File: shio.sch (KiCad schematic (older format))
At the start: 86 parts, among them J1 10118193-0001LF, U1 LM66100DCKT, U2 MAX38640AENT+, U3 NRF52840-CKAA-R7, U4 LM66100DCKT, U5 BMA400, U6 W25N01GVZEIG_TR, U8 SiP32431DR3, Y1 32.768kHz, Y3 32MHz

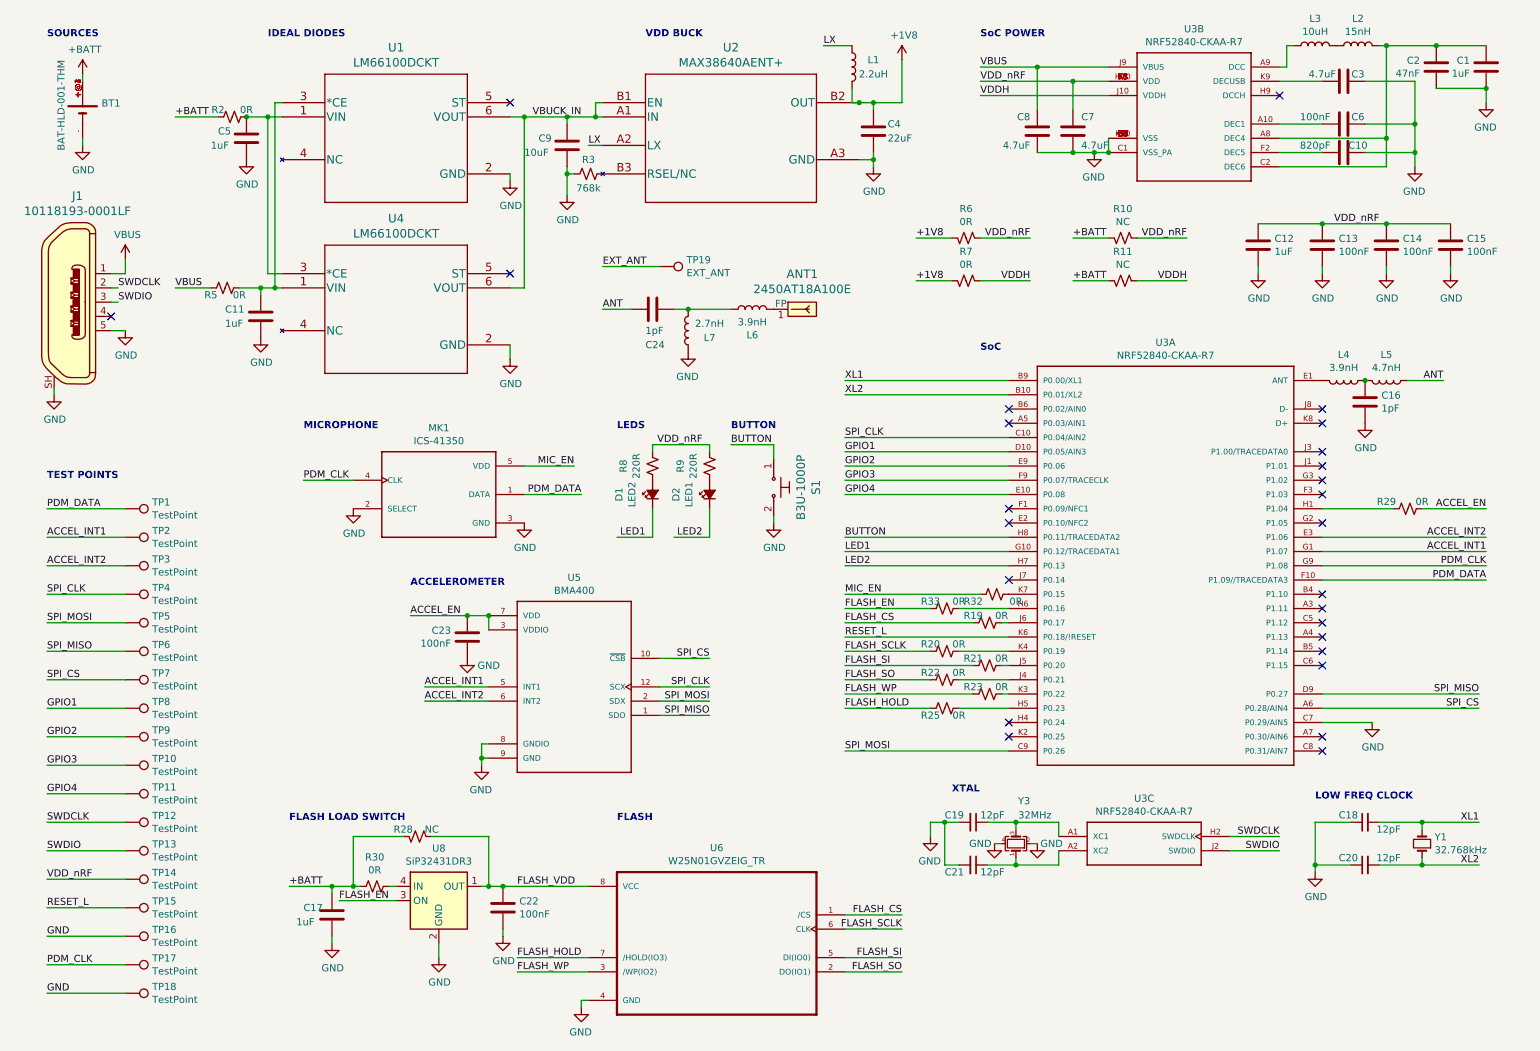
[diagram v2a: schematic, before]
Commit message: placed and routed addtl zero ohms in case powering off gpio doesn't work, prepping for fab
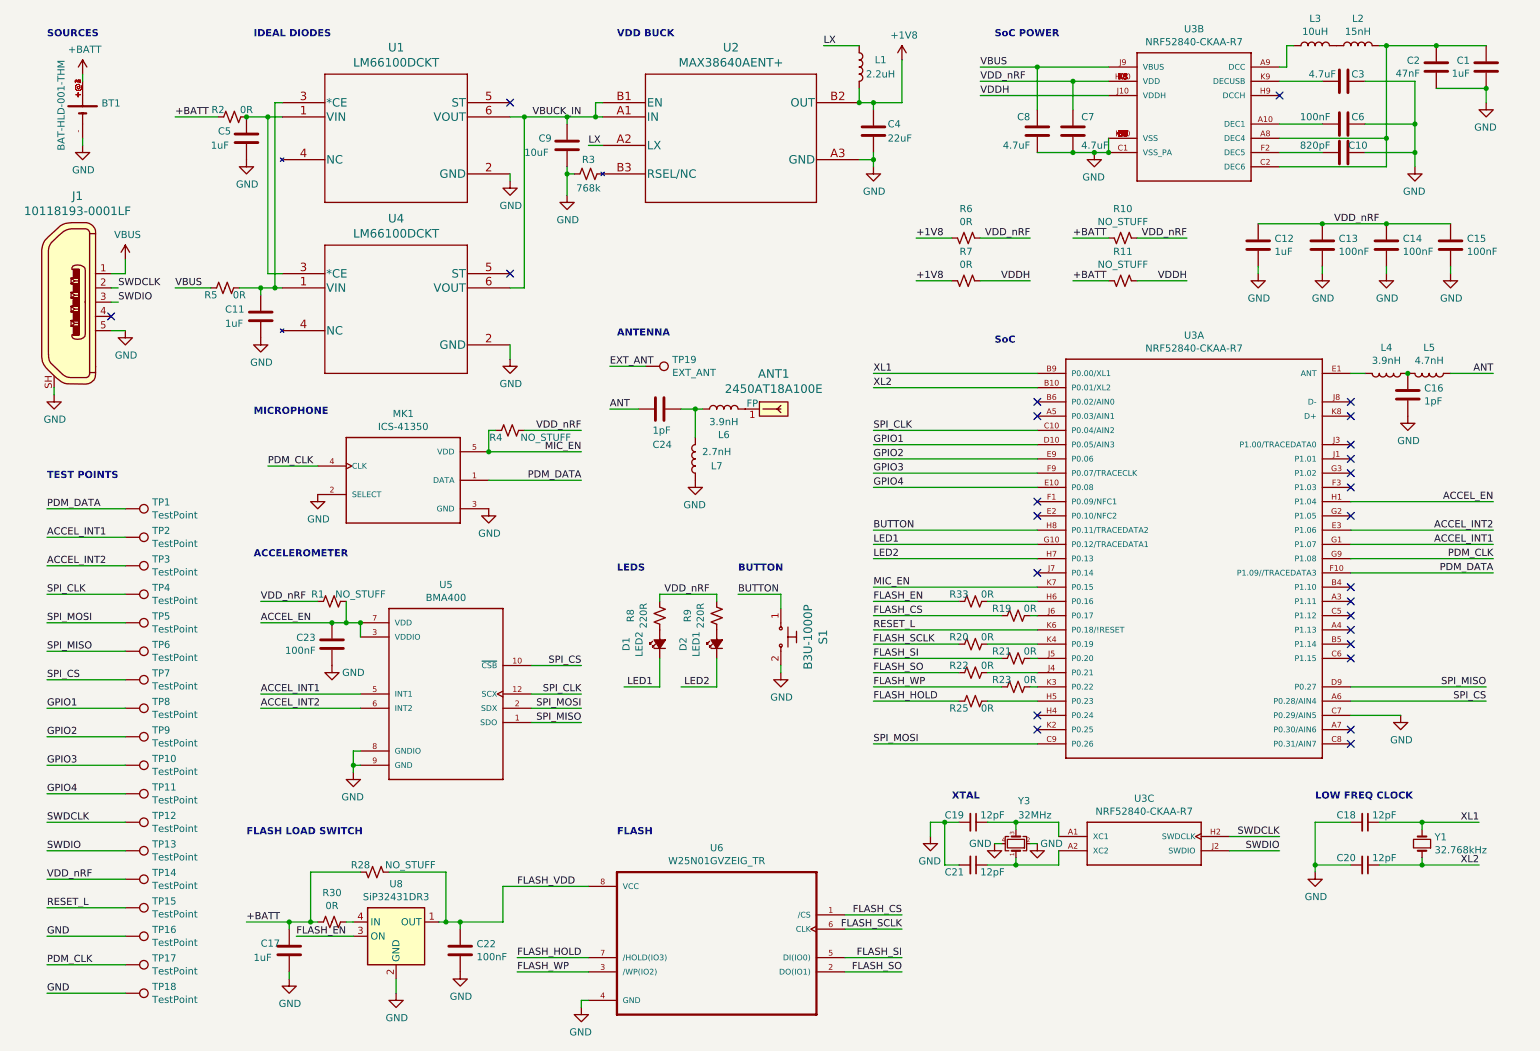
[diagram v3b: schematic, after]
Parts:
- removed R29, R32: 0R, Resistor_SMD:R_0201_0603Metric, symbol Device:R_Small_US
- added R1, R4: NO_STUFF, Resistor_SMD:R_0201_0603Metric, symbol Device:R_Small_US
- BT1: Description (none) -> BATTERY RETAINER COIN PC PIN; MPN (none) -> BAT-HLD-001-THM; Manufacturer (none) -> Linx Technologies Inc.
- C18, C19, C20, C21: Description (none) -> 12pF ±2% 25V Ceramic Capacitor C0G, NP0 0201 (0603 Metric); MPN (none) -> GRM0335C1E120GA01D; Manufacturer (none) -> Murata Electronics
- MK1: Cost (none) -> 1.30 USD; Description (none) -> Bottom Port PDM Low Power muti-Mode Microphone with high AO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; Field4 Bottom Port PDM Low Power muti-Mode Microphone with high AO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 -> (none); Field5 Good -> (none); Field6 ICS-41350 -> (none); Field7 1.30 USD -> (none); Field8 TDK-InvenSense -> (none); MPN (none) -> ICS-41350; Manufacturer (none) -> TDK-InvenSense
- R10, R11, R28: value NC -> NO_STUFF
- U3: Field4 Nordic -> (none); Field5 0.514mm -> (none); Field6 IPC7351B -> (none); MPN (none) -> NRF52840-CKAA-R7; Manufacturer (none) -> Nordic
- U5: Description (none) -> Accelerometer X, Y, Z Axis ±2g, 4g, 8g, 16g 12-LGA _2x2_; Field4 LGA-12 Bosch Tools -> (none); Field5 Bosch Sensortec -> (none); Field7 Unavailable -> None; Field8 Accelerometer X, Y, Z Axis ±2g, 4g, 8g, 16g 12-LGA _2x2_ -> (none); Manufacturer (none) -> Bosch Sensortec; Package (none) -> LGA-12
- U6: Description (none) -> Ic Flash 1gbit 104mhz 8wson; Field4 W25N01GVZEIG TR -> (none); Field5 IPC7351B -> (none); Field6 WSON-8 Winbond -> (none); Field7 Ic Flash 1gbit 104mhz 8wson -> (none); Field8 Winbond Electronics -> (none); Manufacturer (none) -> Winbond Electronics; Package (none) -> WSON-8
- U8: MPN (none) -> SiP32431DR3; Manufacturer (none) -> Vishay Siliconix
- Y1: Description (none) -> XTAL SMD 3215, 32.768kHz, 9pF, ±20ppm; MPN (none) -> NX3215SA-32.768K-STD-MUA-9; Manufacturer (none) -> NDK America, Inc.; Package (none) -> XTAL_3215
- Y3: Description (none) -> 32MHz ±10ppm Crystal 8pF 50 Ohms 4-SMD, No Lead; MPN (none) -> Q 32,0-JXS21-8-10/10-FU-WA-LF; Manufacturer (none) -> Jauch Quartz
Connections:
- net ACCEL_EN: now also U3.H1 (P1.04), R1.2
- net GND: now also C18.2, C20.2; no longer C18.1, C20.1
- net MIC_EN: now also U3.K7 (P0.15), R4.1
- net VDD_nRF: now also R1.1, R4.2
- net XL1: now also C18.1; no longer C18.2
- net XL2: now also C20.1; no longer C20.2
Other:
- note added: "ANTENNA"
- moved on the sheet: ANT1, C16, C17, C22, C23, C24, D1, D2, L1, L4, L5, L6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

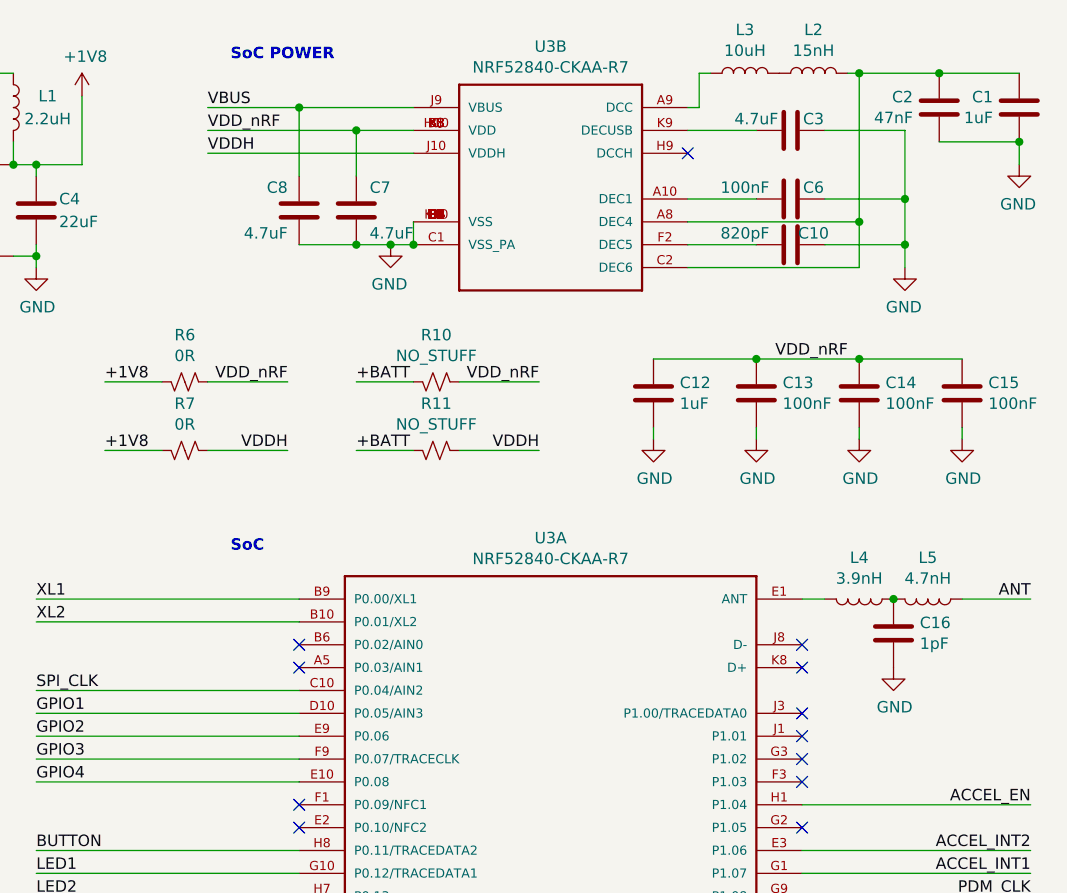
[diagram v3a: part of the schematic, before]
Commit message: continue associating components with orderable parts
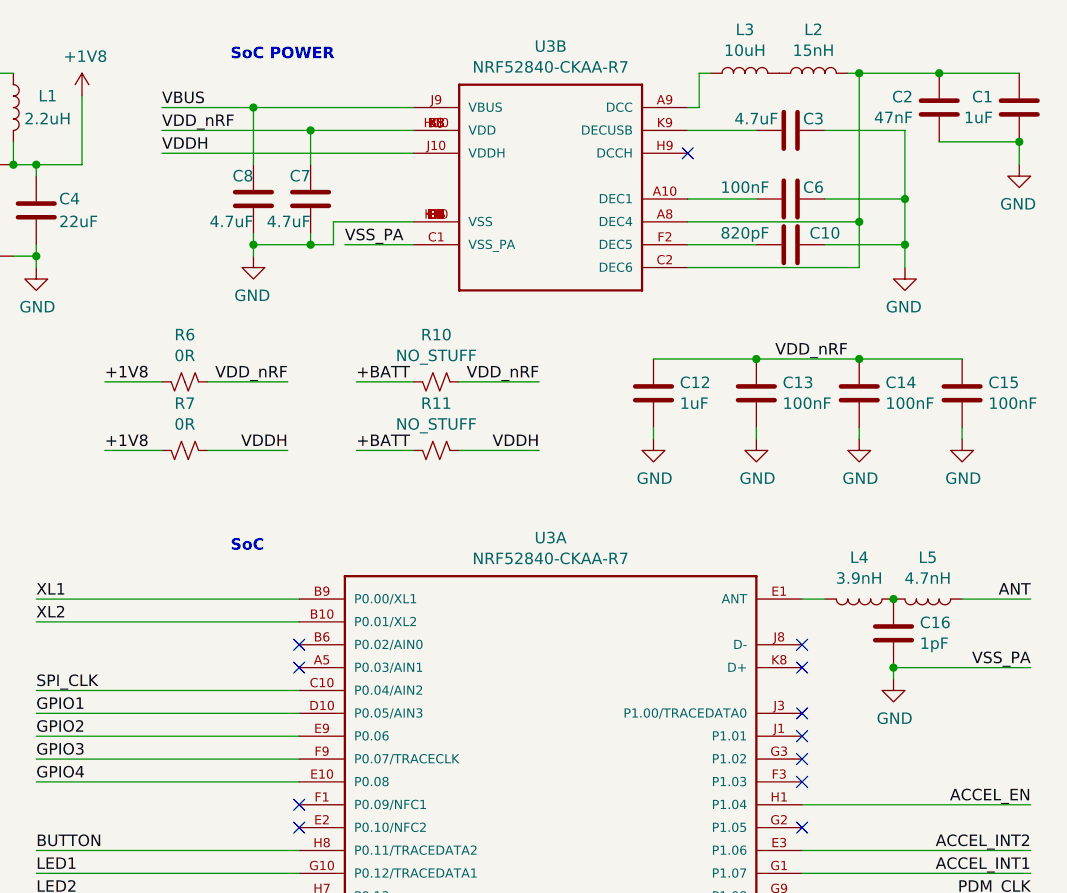
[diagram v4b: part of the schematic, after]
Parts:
- C1, C12, C3, C7: Description (none) -> Capacitor, 0402, X7R, ±10%
- C10, C2: Description (none) -> Capacitor, 0201, X7R, ±10%
- C13, C14, C15: Description (none) -> 0.1µF ±10% 16V Ceramic Capacitor X7S 0201 (0603 Metric); MPN (none) -> GRM033C71C104KE14D; Manufacturer (none) -> Murata Electronics
- C16: Description (none) -> Capacitor, 0201, NP0, ±5%
- C8: Description (none) -> Capacitor, 0402, X7S, ±10%
- L2: Description (none) -> 15nH Unshielded Thick Film Inductor 250mA 700mOhm Max 0201 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; MPN (none) -> LQP03TN15NJ02D; Manufacturer (none) -> Murata Electronics
- L3: Description (none) -> 10µH Shielded Multilayer Inductor 300mA 600mOhm 0603 (1608 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; MPN (none) -> MLZ1608N100LT000; Manufacturer (none) -> TDK
- L4, L5: Description (none) -> High frequency chip inductor ±5%
- U3: Package (none) -> WLCSP-94
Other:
- moved on the sheet: C7, C8

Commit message: adding bom desc
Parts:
- U5: Field6 None -> (none); Field7 None -> (none)
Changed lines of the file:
@@
 F 4 "LGA-12" H 3600 5300 50  0001 L BNN "Package"
 F 5 "Bosch Sensortec" H 3600 5300 50  0001 L BNN "Manufacturer"
-F 6 "None" H 3600 5300 50  0001 L BNN "Field6"
-F 7 "None" H 3600 5300 50  0001 L BNN "Field7"
-F 8 "Accelerometer X, Y, Z Axis ±2g, 4g, 8g, 16g 12-LGA _2x2_" H 3600 5300 50  0001 L BNN "Description"
+F 6 "Accelerometer X, Y, Z Axis ±2g, 4g, 8g, 16g 12-LGA _2x2_" H 3600 5300 50  0001 L BNN "Description"
 	1    3600 5300
 	-1   0    0    -1

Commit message: Add more part descriptions
- Thickened traces between between buck components
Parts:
- C11, C17, C22, C23, C4, C5, C9: Description (none) -> Capacitor, 0201, X5R, ±10%
- C24: Digi-Key_PN (none) -> 500R07S1R0BV4T
- D1: Digi-Key_PN (none) -> 350-4450-1-ND
- D2: Digi-Key_PN (none) -> 350-4448-1-ND
- L1: Description (none) -> 250mA Peak Current
- L6: Digi-Key_PN (none) -> L-07C3N9SV6T
- L7: Digi-Key_PN (none) -> L-07C2N7SV6T
- R3: Description (none) -> 768K OHM 1% 1/20W; Digi-Key_PN (none) -> P123157CT-ND
- R8, R9: Description (none) -> Resistor, ±1%, 0.05W
- U6: Digi-Key_PN (none) -> W25N01GVZEIGCT-ND
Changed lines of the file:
@@
 F 2 "Resistor_SMD:R_0201_0603Metric" H 5500 4750 50  0001 C CNN
 F 3 "~" H 5500 4750 50  0001 C CNN
+F 4 "Resistor, ±1%, 0.05W" V 5500 4750 50  0001 C CNN "Description"
 	1    5500 4750
 	1    0    0    -1
@@
 F 2 "Resistor_SMD:R_0201_0603Metric" H 5100 4750 50  0001 C CNN
 F 3 "~" H 5100 4750 50  0001 C CNN
+F 4 "Resistor, ±1%, 0.05W" V 5100 4750 50  0001 C CNN "Description"
 	1    5100 4750
 	1    0    0    -1
@@
 F 2 "LED_SMD:LED_0402_1005Metric" V 5100 4950 50  0001 C CNN
 F 3 "~" V 5100 4950 50  0001 C CNN
+F 4 "350-4450-1-ND" H 5100 4950 50  0001 C CNN "Digi-Key_PN"
 	1    5100 4950
 	0    -1   -1   0
@@
 F 2 "LED_SMD:LED_0402_1005Metric" V 5500 4950 50  0001 C CNN
 F 3 "~" V 5500 4950 50  0001 C CNN
+F 4 "350-4448-1-ND" H 5500 4950 50  0001 C CNN "Digi-Key_PN"
 	1    5500 4950
 	0    -1   -1   0
@@
 F 2 "Capacitor_SMD:C_0402_1005Metric" H 6638 1200 50  0001 C CNN
 F 3 "~" H 6600 1350 50  0001 C CNN
+F 4 "Capacitor, 0201, X5R, ±10%" H 6600 1350 50  0001 C CNN "Description"
 	1    6600 1350
 	1    0    0    -1
@@
 F 2 "Capacitor_SMD:C_0402_1005Metric" H 4488 1300 50  0001 C CNN
 F 3 "~" H 4450 1450 50  0001 C CNN
+F 4 "Capacitor, 0201, X5R, ±10%" H 4450 1450 50  0001 C CNN "Description"
 	1    4450 1450
 	1    0    0    -1
@@
 F 2 "Capacitor_SMD:C_0402_1005Metric" H 2338 2500 50  0001 C CNN
 F 3 "~" H 2300 2650 50  0001 C CNN
+F 4 "Capacitor, 0201, X5R, ±10%" H 2300 2650 50  0001 C CNN "Description"
 	1    2300 2650
 	1    0    0    -1
@@
 F 2 "Resistor_SMD:R_0201_0603Metric" H 4600 1650 50  0001 C CNN
 F 3 "~" H 4600 1650 50  0001 C CNN
+F 4 "768K OHM 1% 1/20W" V 4600 1650 50  0001 C CNN "Description"
+F 5 "P123157CT-ND" V 4600 1650 50  0001 C CNN "Digi-Key_PN"
 	1    4600 1650
 	0    -1   -1   0
@@
 F 2 "Inductor_SMD:L_0603_1608Metric" H 6500 900 50  0001 C CNN
 F 3 "~" H 6500 900 50  0001 C CNN
+F 4 "250mA Peak Current" H 6500 900 50  0001 C CNN "Description"
 	1    6500 900
 	1    0    0    -1
@@
 F 2 "Capacitor_SMD:C_0402_1005Metric" H 2238 1250 50  0001 C CNN
 F 3 "~" H 2200 1400 50  0001 C CNN
+F 4 "Capacitor, 0201, X5R, ±10%" H 2200 1400 50  0001 C CNN "Description"
 	1    2200 1400
 	1    0    0    -1
@@
 F 7 "Ic Flash 1gbit 104mhz 8wson" H 5500 7050 50  0001 L BNN "Description"
 F 8 "Winbond Electronics" H 5500 7050 50  0001 L BNN "Manufacturer"
+F 9 "W25N01GVZEIGCT-ND" H 5500 7050 50  0001 C CNN "Digi-Key_PN"
 	1    5500 7050
 	-1   0    0    -1
@@
 F 2 "Capacitor_SMD:C_0402_1005Metric" H 2538 6950 50  0001 C CNN
 F 3 "~" H 2500 7100 50  0001 C CNN
+F 4 "Capacitor, 0201, X5R, ±10%" H 2500 7100 50  0001 C CNN "Description"
 	1    2500 7100
 	1    0    0    -1
@@
 F 2 "Capacitor_SMD:C_0201_0603Metric" H 5138 3150 50  0001 C CNN
 F 3 "~" H 5100 3300 50  0001 C CNN
+F 4 "500R07S1R0BV4T" V 5100 3300 50  0001 C CNN "Digi-Key_PN"
 	1    5100 3300
 	0    1    1    0
@@
 F 2 "Capacitor_SMD:C_0201_0603Metric" H 2838 4800 50  0001 C CNN
 F 3 "~" H 2800 4950 50  0001 C CNN
+F 4 "Capacitor, 0201, X5R, ±10%" H 2800 4950 50  0001 C CNN "Description"
 	1    2800 4950
 	-1   0    0    -1
@@
 F 2 "Inductor_SMD:L_0201_0603Metric" H 5550 3300 50  0001 C CNN
 F 3 "~" H 5550 3300 50  0001 C CNN
+F 4 "L-07C3N9SV6T" V 5550 3300 50  0001 C CNN "Digi-Key_PN"
 	1    5550 3300
 	0    -1   -1   0
@@
 F 2 "Inductor_SMD:L_0201_0603Metric" H 5350 3650 50  0001 C CNN
 F 3 "~" H 5350 3650 50  0001 C CNN
+F 4 "L-07C2N7SV6T " H 5350 3650 50  0001 C CNN "Digi-Key_PN"
 	1    5350 3650
 	-1   0    0    1
@@
 F 2 "Capacitor_SMD:C_0201_0603Metric" H 3738 6950 50  0001 C CNN
 F 3 "~" H 3700 7100 50  0001 C CNN
+F 4 "Capacitor, 0201, X5R, ±10%" H 3700 7100 50  0001 C CNN "Description"
 	1    3700 7100
 	1    0    0    -1

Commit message: Add final part descriptions
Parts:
- C6: Description (none) -> Capacitor, X7R, ±10%
- U1, U4: Digi-Key_PN (none) -> 296-53540-1-ND
- U2: value MAX38640AENT+ -> MAX38640AENT+T; MPN (none) -> MAX38640AENT+T
- U5: Digi-Key_PN (none) -> 828-1081-1-ND; MPN (none) -> BMA400
- U6: MPN (none) -> W25N01GVZEIG TR
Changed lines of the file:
@@
 F 2 "Capacitor_SMD:C_0201_0603Metric" H 9938 1150 50  0001 C CNN
 F 3 "~" H 9900 1300 50  0001 C CNN
+F 4 "Capacitor, X7R, ±10%" V 9900 1300 50  0001 C CNN "Description"
 	1    9900 1300
 	0    -1   1    0
@@
 F 1 "LM66100DCKT" H 3250 2631 60  0000 C CNN
 F 2 "Shio:LM66100DCKT" H 3250 2590 60  0001 C CNN
-F 3 "" H 2450 2350 60  0000 C CNN
+F 3 "https://www.ti.com/lit/ds/symlink/lm66100.pdf?HQS=TI-null-null-digikeymode-df-pf-null-wwe&ts=1591950231750" H 2450 2350 60  0001 C CNN
+F 4 "296-53540-1-ND" H 2450 2350 50  0001 C CNN "Digi-Key_PN"
 	1    2450 2350
 	1    0    0    -1
@@
 F 1 "LM66100DCKT" H 3250 1431 60  0000 C CNN
 F 2 "Shio:LM66100DCKT" H 3250 1390 60  0001 C CNN
-F 3 "" H 2450 1150 60  0000 C CNN
+F 3 "https://www.ti.com/lit/ds/symlink/lm66100.pdf?HQS=TI-null-null-digikeymode-df-pf-null-wwe&ts=1591950231750" H 2450 1150 60  0001 C CNN
+F 4 "296-53540-1-ND" H 2450 1150 50  0001 C CNN "Digi-Key_PN"
 	1    2450 1150
 	1    0    0    -1
@@
 P 4700 1150
 F 0 "U2" H 5600 1537 60  0000 C CNN
-F 1 "MAX38640AENT+" H 5600 1431 60  0000 C CNN
+F 1 "MAX38640AENT+T" H 5600 1431 60  0000 C CNN
 F 2 "Shio:MAX38640AENT&plus_" H 5600 1390 60  0001 C CNN
-F 3 "" H 4700 1150 60  0000 C CNN
+F 3 "https://www.mouser.com/datasheet/2/256/MAX38640A-MAX38643B-1622807.pdf" H 4700 1150 60  0001 C CNN
+F 4 "MAX38640AENT+T" H 4700 1150 50  0001 C CNN "MPN"
 	1    4700 1150
 	1    0    0    -1
@@
 F 2 "Shio:SON127P800X600X80-9N" H 5500 7050 50  0001 L BNN
 F 3 "" H 5500 7050 50  0001 L BNN
-F 4 "" H 5500 7050 50  0001 L BNN "Field4"
+F 4 "W25N01GVZEIG TR" H 5500 7050 50  0001 L BNN "MPN"
 F 5 "" H 5500 7050 50  0001 L BNN "Field5"
 F 6 "WSON-8" H 5500 7050 50  0001 L BNN "Package"
@@
 F 5 "Bosch Sensortec" H 3600 5300 50  0001 L BNN "Manufacturer"
 F 6 "Accelerometer X, Y, Z Axis ±2g, 4g, 8g, 16g 12-LGA _2x2_" H 3600 5300 50  0001 L BNN "Description"
+F 7 "828-1081-1-ND" H 3600 5300 50  0001 C CNN "Digi-Key_PN"
+F 8 "BMA400" H 3600 5300 50  0001 C CNN "MPN"
 	1    3600 5300
 	-1   0    0    -1

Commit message: Modified component descriptions to match resistor sizes
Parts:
- C11, C17, C4, C9: Description Capacitor, 0201, X5R, ±10% -> Capacitor, 0402, X5R, ±10%
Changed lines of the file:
@@
 F 2 "Capacitor_SMD:C_0402_1005Metric" H 6638 1200 50  0001 C CNN
 F 3 "~" H 6600 1350 50  0001 C CNN
-F 4 "Capacitor, 0201, X5R, ±10%" H 6600 1350 50  0001 C CNN "Description"
+F 4 "Capacitor, 0402, X5R, ±10%" H 6600 1350 50  0001 C CNN "Description"
 	1    6600 1350
 	1    0    0    -1
@@
 F 2 "Capacitor_SMD:C_0402_1005Metric" H 4488 1300 50  0001 C CNN
 F 3 "~" H 4450 1450 50  0001 C CNN
-F 4 "Capacitor, 0201, X5R, ±10%" H 4450 1450 50  0001 C CNN "Description"
+F 4 "Capacitor, 0402, X5R, ±10%" H 4450 1450 50  0001 C CNN "Description"
 	1    4450 1450
 	1    0    0    -1
@@
 F 2 "Capacitor_SMD:C_0402_1005Metric" H 2338 2500 50  0001 C CNN
 F 3 "~" H 2300 2650 50  0001 C CNN
-F 4 "Capacitor, 0201, X5R, ±10%" H 2300 2650 50  0001 C CNN "Description"
+F 4 "Capacitor, 0402, X5R, ±10%" H 2300 2650 50  0001 C CNN "Description"
 	1    2300 2650
 	1    0    0    -1
@@
 F 2 "Capacitor_SMD:C_0402_1005Metric" H 2538 6950 50  0001 C CNN
 F 3 "~" H 2500 7100 50  0001 C CNN
-F 4 "Capacitor, 0201, X5R, ±10%" H 2500 7100 50  0001 C CNN "Description"
+F 4 "Capacitor, 0402, X5R, ±10%" H 2500 7100 50  0001 C CNN "Description"
 	1    2500 7100
 	1    0    0    -1
